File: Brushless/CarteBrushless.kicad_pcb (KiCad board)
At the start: 2 copper layers, 100 x 157 mm, 69 parts, among them J1 Conn_01x03_Pin, J2 Conn_01x03_Pin, J3 Conn_01x03_Pin, Q2 IRF7424, U1 STM32G484RETx, U2 TCAN332G

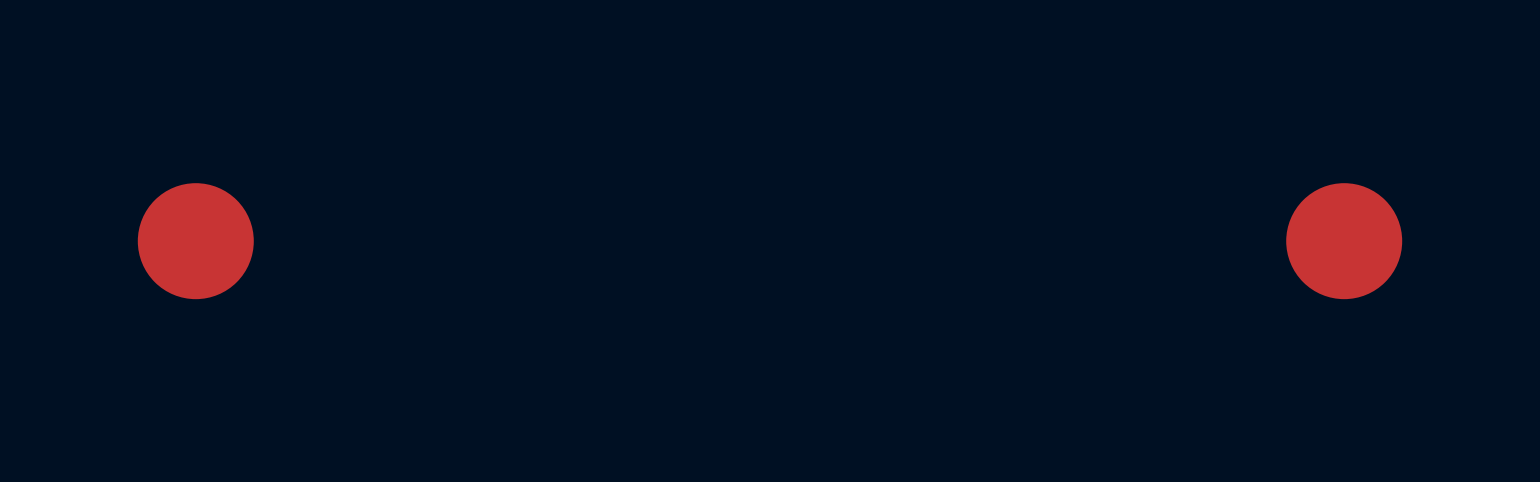
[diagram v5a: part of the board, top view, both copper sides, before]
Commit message: resistance LED + schema soudure
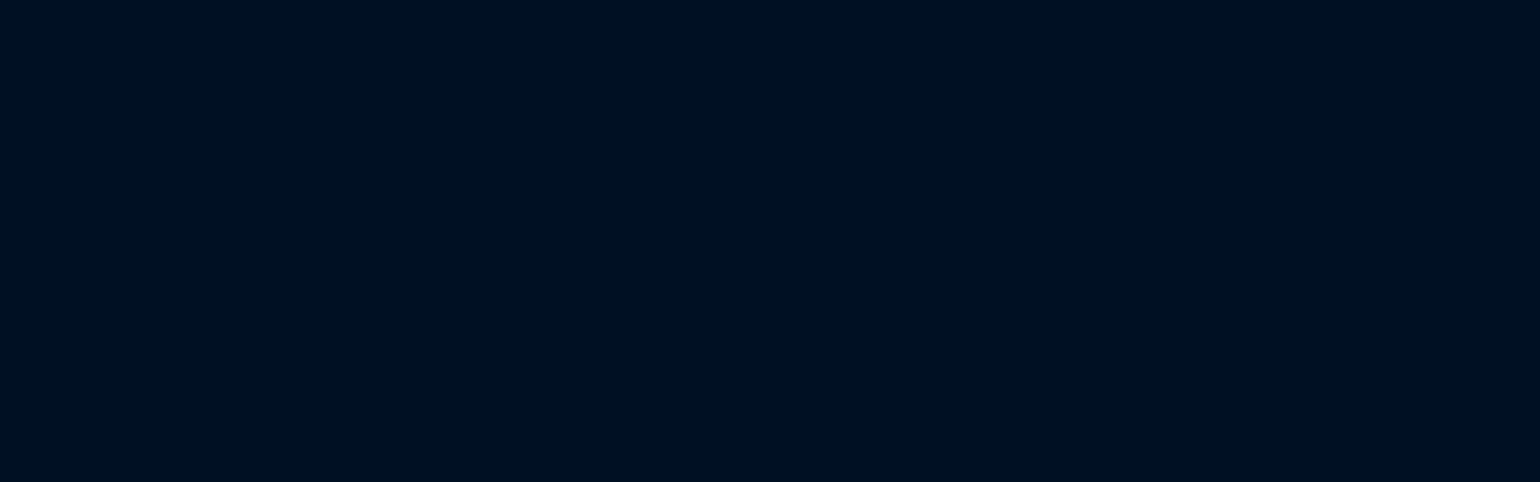
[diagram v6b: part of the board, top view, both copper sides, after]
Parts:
- removed REF** (x2): EC-Registration, ENAC_robotique:EC-Registration
- R10, R6: value osef -> 500
- R5: value osef -> 850
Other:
- board text added: "-"
- board text added: "Bouton"
- board text added: "Diode"
- board text added: "IRF7424"
- board text added: "LED"
- board text added: "LM3940IMP"
- board text added: "R-78E5.0-1.0"
- board text added: "TCAN332G"
- board text added: "ZENER"
